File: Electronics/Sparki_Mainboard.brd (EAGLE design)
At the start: 65 x 92.9 mm, 92 parts, among them IC1 74595, IC2 74595, J1 1X2-3.5MM, U2 ATMEGA32U4-AU, U3 LP2985-33DBVR, U4 MMA8452Q, U5 NRF24L01SMD, X1 USBSMD, X3 05-JST-B5B-XH-A, X4 05-XH-JST-B5B-XH-A, X5 05-JST-B5B-XH-A, Y1 ANTENNA2SMD5

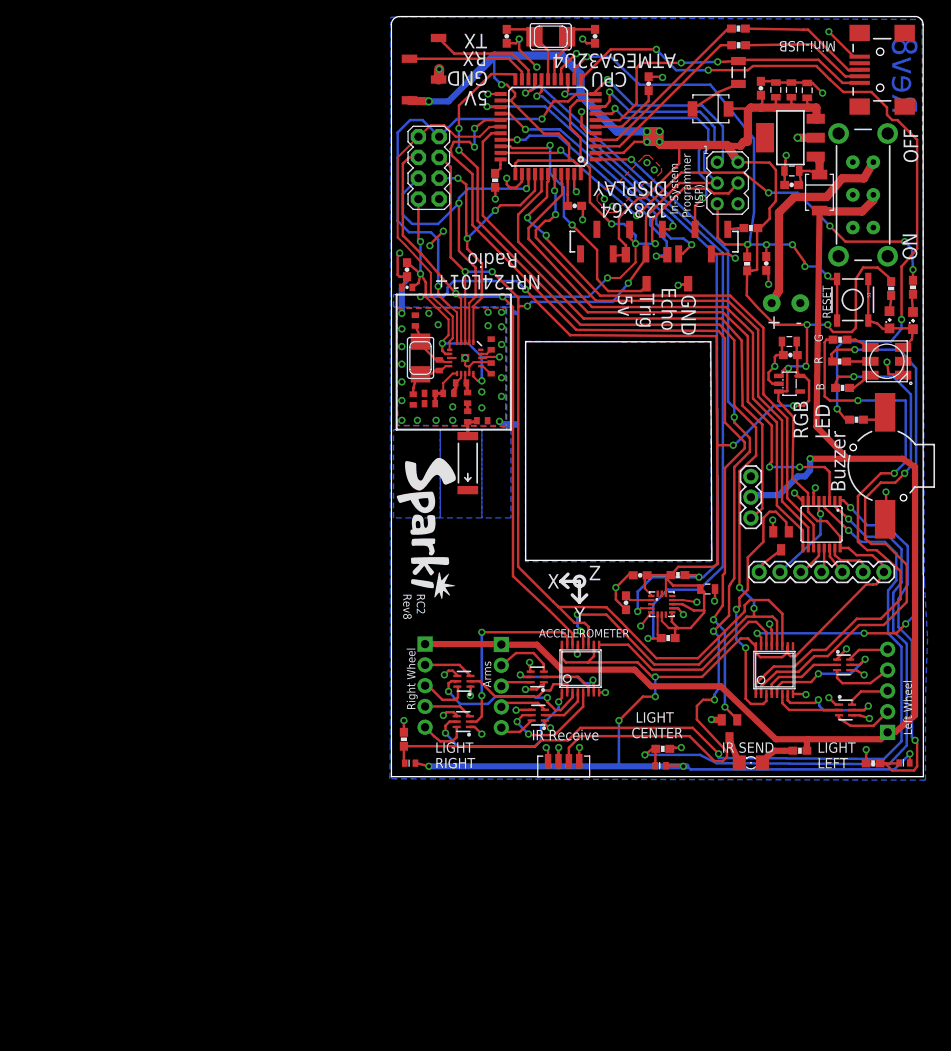
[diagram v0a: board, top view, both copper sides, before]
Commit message: Updated connectors, sensor multiplexing
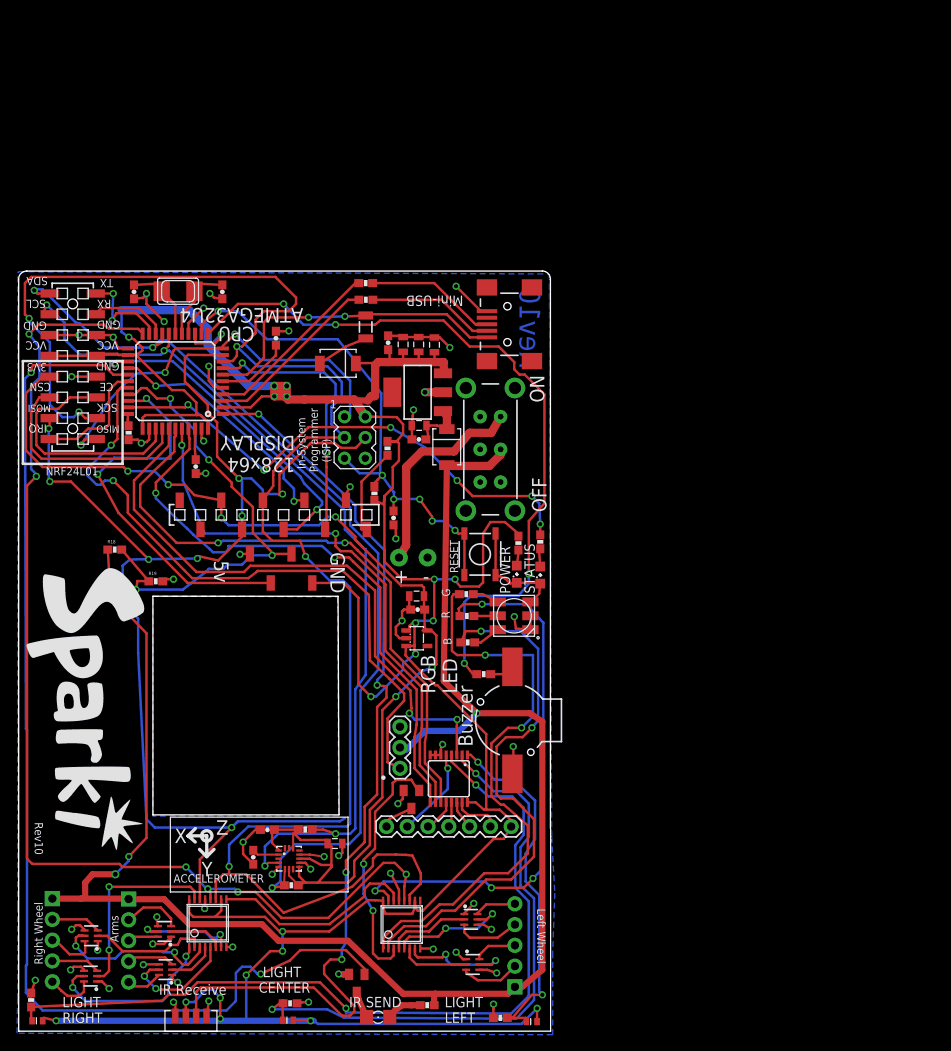
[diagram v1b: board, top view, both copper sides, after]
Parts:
- removed BLUETOOTH: Bluetooth, arcbotics:1X04-2.54MM-SMD
- removed C17: 10uF, SparkFun-Capacitors:0603-CAP
- removed C18: 0.1uF, SparkFun-Capacitors:0402-CAP
- removed C19, C20: 8pf, SparkFun:C0402
- removed C21: 33nF, SparkFun:C0402
- removed C22: 2.2nF, SparkFun:C0402
- removed C23: 4.7pF, SparkFun:C0402
- removed C24: 1.0pF, SparkFun:C0402
- removed C25: 1.5pF, SparkFun:C0402
- removed L1: 3.9nH, SparkFun:C0402
- removed L2: 2.7nH, SparkFun:C0402
- removed L3: 8.2nH, SparkFun:C0402
- removed R16: 1M, SparkFun:C0402
- removed R17: 22K, SparkFun:C0402
- removed U$9: M04X2, SparkFun-Connectors:2X4
- removed U5: NRF24L01SMD, SparkFun:QFN20
- removed X6: (no value), adafruit:NX5032
- removed Y1: ANTENNA2SMD5, SparkFun:ANTENNA-CHIP5
- added R18, R19: 100, SparkFun-Passives:0603-RES
- added U$10: M08X2SMD, arcbotics:2X08-2.54MM-SMD
- JP2: value M102MMSMD -> M10; device SparkFun-Connectors:1X10-2MM-SMD -> arcbotics:1X10-2.54MM-SMD
- R11, R12, R13: value 10k -> 47k
- moved SONIC 64.9 mm to (28.6, 56.6), turned to 0 degrees
- moved JP2 59.3 mm to (20.0, 63.1)
- moved C8 56.2 mm to (21.9, 69.0), turned to 270 degrees
- moved R13 55.6 mm to (1.81, 3.82)
- moved U$3 55.5 mm to (63.0, 1.17)
- moved U$4 55.4 mm to (2.57, 1.28)
- moved R9 55.4 mm to (55.2, 47.5)
- moved R8 55.3 mm to (55.0, 53.4)
- moved C4 55.2 mm to (14.4, 90.4)
- moved C6 55.2 mm to (25.2, 90.4)
- moved C10 55.2 mm to (49.2, 74.0)
- moved D1 55.2 mm to (39.3, 81.6)
- moved R1 55.2 mm to (42.7, 91.4)
- moved X2 55.2 mm to (19.8, 90.5)
- moved C13 55.2 mm to (29.0, 21.3)
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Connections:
- net LINE_MID renamed LINE_CENTER
- net PD5 renamed N$13
- removed net ANT: C24.2, C25.2, Y1.FEED
- removed net N$20: C19.1, R16.1, U5.9, X6.P$2
- removed net N$23: C20.1, R16.2, U5.10, X6.P$1
- removed net N$24: L1.1, L3.2, U5.13
- removed net N$25: C22.1, C23.1, L2.1, U5.11
- removed net N$27: R17.1, U5.16
- removed net N$28: C21.1, U5.19
- removed net N$33: L2.2, L3.1, U5.12
- removed net N$34: C25.1, L1.2
- net GND: now also R19.2, U$10.10, U$10.5, U$10.6, U$6.7; no longer BLUETOOTH.2, C17.2, C18.2, C19.2, C20.2, C21.2, C22.2, C23.2, C24.1, R17.2, U$9.1, U5.0, U5.14, U5.17, U5.20, U5.8
- net MISO: now also U$10.16; no longer U$9.7, U5.5
- net MOSI: now also U$10.13; no longer U$9.6, U5.4
- net PB4: now also U$10.15; no longer U$9.8, U5.6
- net PB6: now also R18.2, R19.1, SONIC.2; no longer SONIC.3
- net PC6: now also SONIC.3; no longer SONIC.2
- net PD0: now also U$10.3
- net PD1: now also U$10.1
- net PF6: now also U$10.11; no longer U$9.3, U5.1
- net PF7: now also U$10.12; no longer U$9.4, U5.2
- net RX: now also U$10.4; no longer BLUETOOTH.4
- net SCK: now also U$10.14; no longer U$9.5, U5.3
- net TX: now also U$10.2; no longer BLUETOOTH.3
- net VCC: now also U$10.7, U$10.8; no longer BLUETOOTH.1, JP2.3, U$6.7
- net VCC_3V3: now also JP2.3, U$10.9; no longer C17.1, C18.1, U$9.2, U5.15, U5.18, U5.7
- net V_BATT_POWER: now also R18.1
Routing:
- net V_BATT_POWER: track 161.0 -> 207.0 mm, vias 1 -> 3
- net SCK: track 176.3 -> 213.1 mm, vias 5 -> 4
- net MISO: track 82.3 -> 49.7 mm
- net PD7: track 106.9 -> 138.7 mm, vias 4 -> 2
- net PB6: track 30.8 -> 58.5 mm, vias 2 -> 4
- net PB4: track 41.7 -> 14.9 mm
- net PD0: track 86.7 -> 111.9 mm, vias 3 -> 4
- net VCC_3V3: track 168.9 -> 146.8 mm, vias 9 -> 6
- net PD1: track 92.9 -> 114.9 mm, vias 2 -> 3
- net VCC: track 374.7 -> 396.4 mm, vias 18 -> 21
- net PC6: track 32.2 -> 48.3 mm
- net MOSI: track 143.8 -> 159.1 mm, vias 6 -> 8
- net PF7: track 43.0 -> 29.2 mm, vias 2 -> 0
- net GND: track 163.6 -> 152.5 mm, vias 81 -> 52
- net PF6: track 36.8 -> 26.8 mm, vias 3 -> 0
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- removed copper zone on layer 1, net GND
- removed copper zone on layer 16, net N$13 (its old number)
- removed copper zone on layer 16, net N$35
- removed copper zone on layer 16, net N$36
- removed copper zone on layer 16, net N$37
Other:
- board text added: "3V3"
- board text added: "C:/Program Files (x86)/EAGLE-6.3.0/Sparki Logo BW.bmp"
- board text added: "CE"
- board text added: "CSN"
- board text added: "IRQ"
- board text added: "MISO"
- board text added: "MOSI"
- board text added: "NRF24L01"
- board text added: "Rev10"
- board text added: "SCK"
- board text added: "SCL"
- board text added: "SDA"
- board text added: "VCC"
- board text removed: "5V"
- board text removed: "Echo"
- board text removed: "NRF24L01+"
- board text removed: "RC2"
- board text removed: "Radio"
- board text removed: "Rev8"
- board text removed: "Trig"
